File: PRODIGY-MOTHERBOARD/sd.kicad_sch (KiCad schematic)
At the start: 1 part, among them J13 Micro_SD_Card_Det2

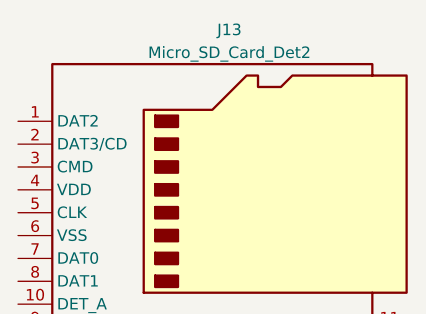
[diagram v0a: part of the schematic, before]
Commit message: project restructure done. Hierarchical sheet done. Outputs/breakouts sheet done
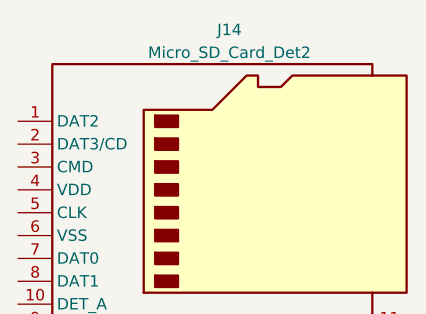
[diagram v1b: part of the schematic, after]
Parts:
- renumbered J13 to J14
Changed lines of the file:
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@@
-(kicad_sch (version 20230121) (generator eeschema)
-  (paper "A4")
-  (symbol (lib_id "Connector:Micro_SD_Card_Det2") (at 154.94 97.79 0) (unit 1)
-    (in_bom yes) (on_board yes) (dnp no) (fields_autoplaced)
-    (property "Reference" "J13" (at 155.575 77.47 0)
-      (effects (font (size 1.27 1.27)))
-    )
-    (property "Value" "Micro_SD_Card_Det2" (at 155.575 80.01 0)
-      (effects (font (size 1.27 1.27)))
-    )
-    (property "Footprint" "Connector_Card:microSD_HC_Hirose_DM3AT-SF-PEJM5" (at 207.01 80.01 0)
-      (effects (font (size 1.27 1.27)) hide)
-    )
-    (property "Datasheet" "https://www.hirose.com/en/product/document?clcode=&productname=&series=DM3&documenttype=Catalog&lang=en&documentid=D49662_en" (at 157.48 95.25 0)
-      (effects (font (size 1.27 1.27)) hide)
-    )
-    (property "JLCPCB" "" (at 154.94 97.79 0)
-      (effects (font (size 1.27 1.27)) hide)
-    )
-    (pin "1")
-    (pin "10")
-    (pin "11")
-    (pin "2")
-    (pin "3")
-    (pin "4")
-    (pin "5")
-    (pin "6")
-    (pin "7")
-    (pin "8")
-    (pin "9")
-    (instances
-      (project "PRODIGY-MOTHERBOARD"
-        (path "/f1c25860-8989-4190-bd24-2491d23ca7d9/33b59e3c-6456-4c33-9606-114445a2e2ee"
-          (reference "J13") (unit 1)
-        )
-      )
-    )
-  )
+(kicad_sch
+	(version 20231120)
+	(generator "eeschema")
+	(generator_version "8.0")
+	(paper "A4")
+	(symbol
+		(lib_id "Connector:Micro_SD_Card_Det2")
+		(at 154.94 97.79 0)
+		(unit 1)
+		(exclude_from_sim no)
+		(in_bom yes)
+		(on_board yes)
+		(dnp no)
+		(fields_autoplaced yes)
+		(property "Reference" "J14"
+			(at 155.575 77.47 0)
+			(effects
+				(font
+					(size 1.27 1.27)
+				)
+			)
+		)
+		(property "Value" "Micro_SD_Card_Det2"
+			(at 155.575 80.01 0)
+			(effects
+				(font
+					(size 1.27 1.27)
+				)
+			)
+		)
+		(property "Footprint" "Connector_Card:microSD_HC_Hirose_DM3AT-SF-PEJM5"
+			(at 207.01 80.01 0)
+			(effects
+				(font
+					(size 1.27 1.27)
+				)
+				(hide yes)
+			)
+		)
+		(property "Datasheet" "https://www.hirose.com/en/product/document?clcode=&productname=&series=DM3&documenttype=Catalog&lang=en&documentid=D49662_en"
+			(at 157.48 95.25 0)
+			(effects
+				(font
+					(size 1.27 1.27)
+				)
+				(hide yes)
+			)
+		)
+		(property "Description" ""
+			(at 154.94 97.79 0)
+			(effects
+				(font
+					(size 1.27 1.27)
+				)
+				(hide yes)
+			)
+		)
+		(property "JLCPCB" ""
+			(at 154.94 97.79 0)
+			(effects
+				(font
+					(size 1.27 1.27)
+				)
+				(hide yes)
+			)
+		)
+		(pin "1"
+		)
+		(pin "10"
+		)
+		(pin "11"
+		)
+		(pin "2"
+		)
+		(pin "3"
+		)
+		(pin "4"
+		)
+		(pin "5"
+		)
+		(pin "6"
+		)
+		(pin "7"
+		)
+		(pin "8"
+		)
+		(pin "9"
+		)
+		(instances
+			(project "PRODIGY-MOTHERBOARD"
+				(path "/f1c25860-8989-4190-bd24-2491d23ca7d9/e2913798-f444-47a6-8b64-53020d7d816b/c4f3c4b1-d676-4f7b-883c-6fdba835d106"
+					(reference "J14")
+					(unit 1)
+				)
+			)
+		)
+	)
 )

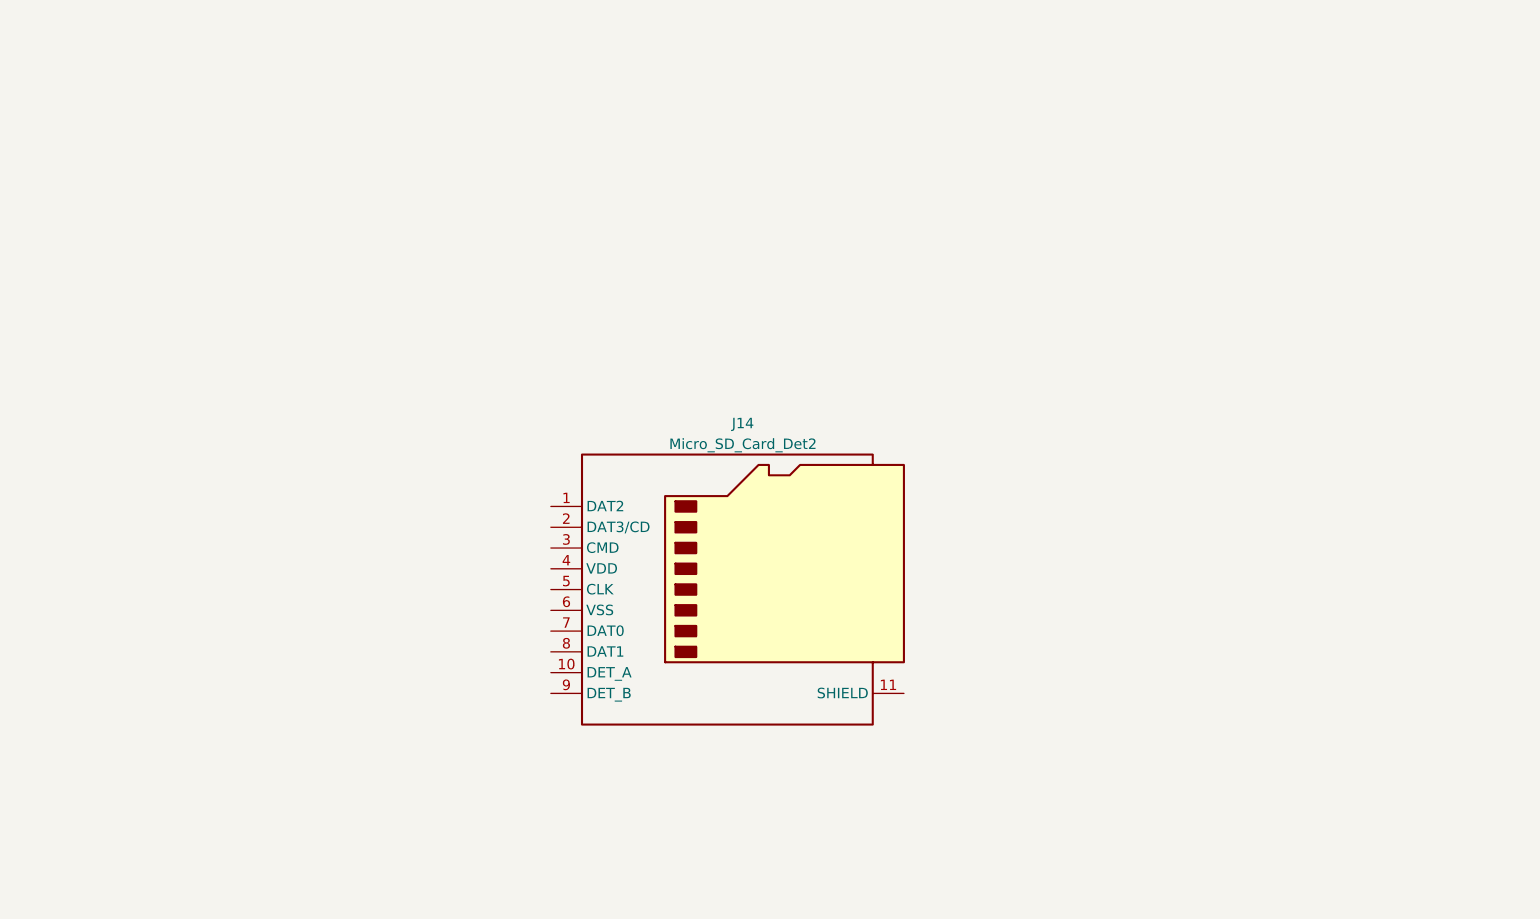
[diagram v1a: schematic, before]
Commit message: SPI SD CARD circuit added.
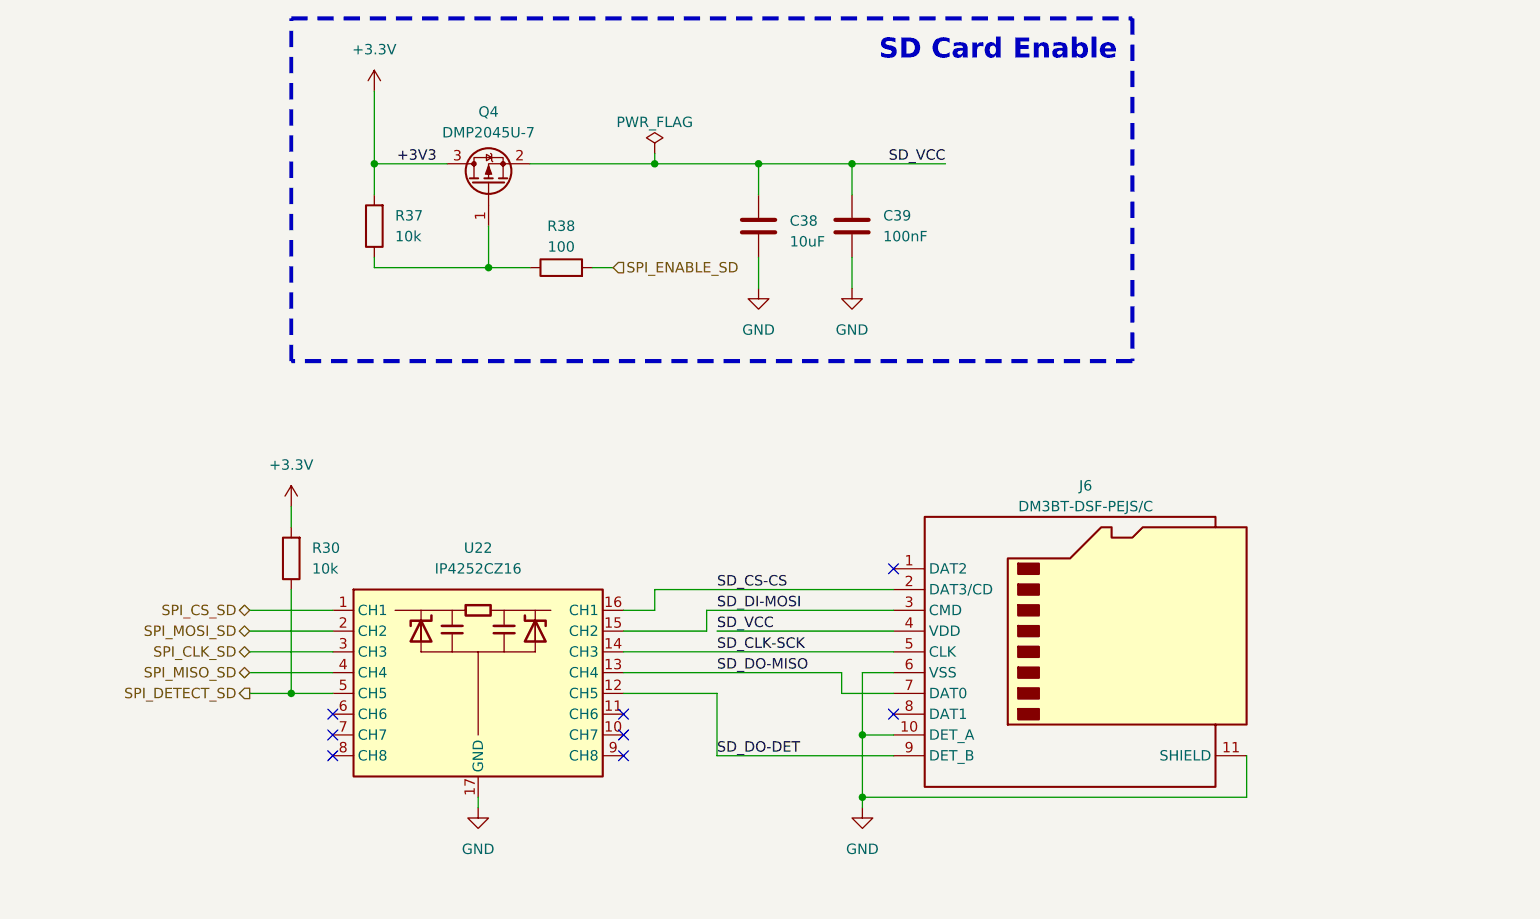
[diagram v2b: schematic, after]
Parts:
- removed J14: Micro_SD_Card_Det2, Connector_Card:microSD_HC_Hirose_DM3AT-SF-PEJM5, symbol Connector:Micro_SD_Card_Det2
- added C38: 10uF, Capacitor_SMD:C_1206_3216Metric, symbol Device:C
- added C39: 100nF, Capacitor_SMD:C_0805_2012Metric, symbol Device:C
- added J6: DM3BT-DSF-PEJS/C, Connector_Card:microSD_HC_Hirose_DM3BT-DSF-PEJS, symbol Connector:Micro_SD_Card_Det2
- added Q4: DMP2045U-7, Package_TO_SOT_SMD:SOT-23, symbol Transistor_FET:IRLML6402
- added R30, R37: 10k, Resistor_SMD:R_0603_1608Metric, symbol Device:R
- added R38: 100, Resistor_SMD:R_0603_1608Metric, symbol Device:R
- added U22: IP4252CZ16, Package_SON:Nexperia_HUSON-16_USON-16-1EP_1.35x3.3mm_P0.4mm_EP0.4x2.8mm, symbol Power_Protection:IP4252CZ16
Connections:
- new net: Q4.1 (G), R37.1, R38.1
- new net +3.3V: Q4.3 (D), R30.2, R37.2
- new net GND: C38.2, C39.2, J6.10 (DET_A), J6.11 (SHIELD), J6.6 (VSS), U22.17 (GND)
- new net SD_CLK-SCK: J6.5 (CLK), U22.14 (CH3)
- new net SD_CS-CS: J6.2 (DAT3/CD), U22.16 (CH1)
- new net SD_DI-MOSI: J6.3 (CMD), U22.15 (CH2)
- new net SD_DO-DET: J6.9 (DET_B), U22.12 (CH5)
- new net SD_DO-MISO: J6.7 (DAT0), U22.13 (CH4)
- new net SD_VCC: C38.1, C39.1, J6.4 (VDD), Q4.2 (S)
- new net SPI_CLK_SD: U22.3 (CH3)
- new net SPI_CS_SD: U22.1 (CH1)
- new net SPI_DETECT_SD: R30.1, U22.5 (CH5)
- new net SPI_ENABLE_SD: R38.2
- new net SPI_MISO_SD: U22.4 (CH4)
- new net SPI_MOSI_SD: U22.2 (CH2)
- no-connect marks 0 -> 8
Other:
- note added: "SD Card Enable"

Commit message: Finished neopixel and button's schematic.
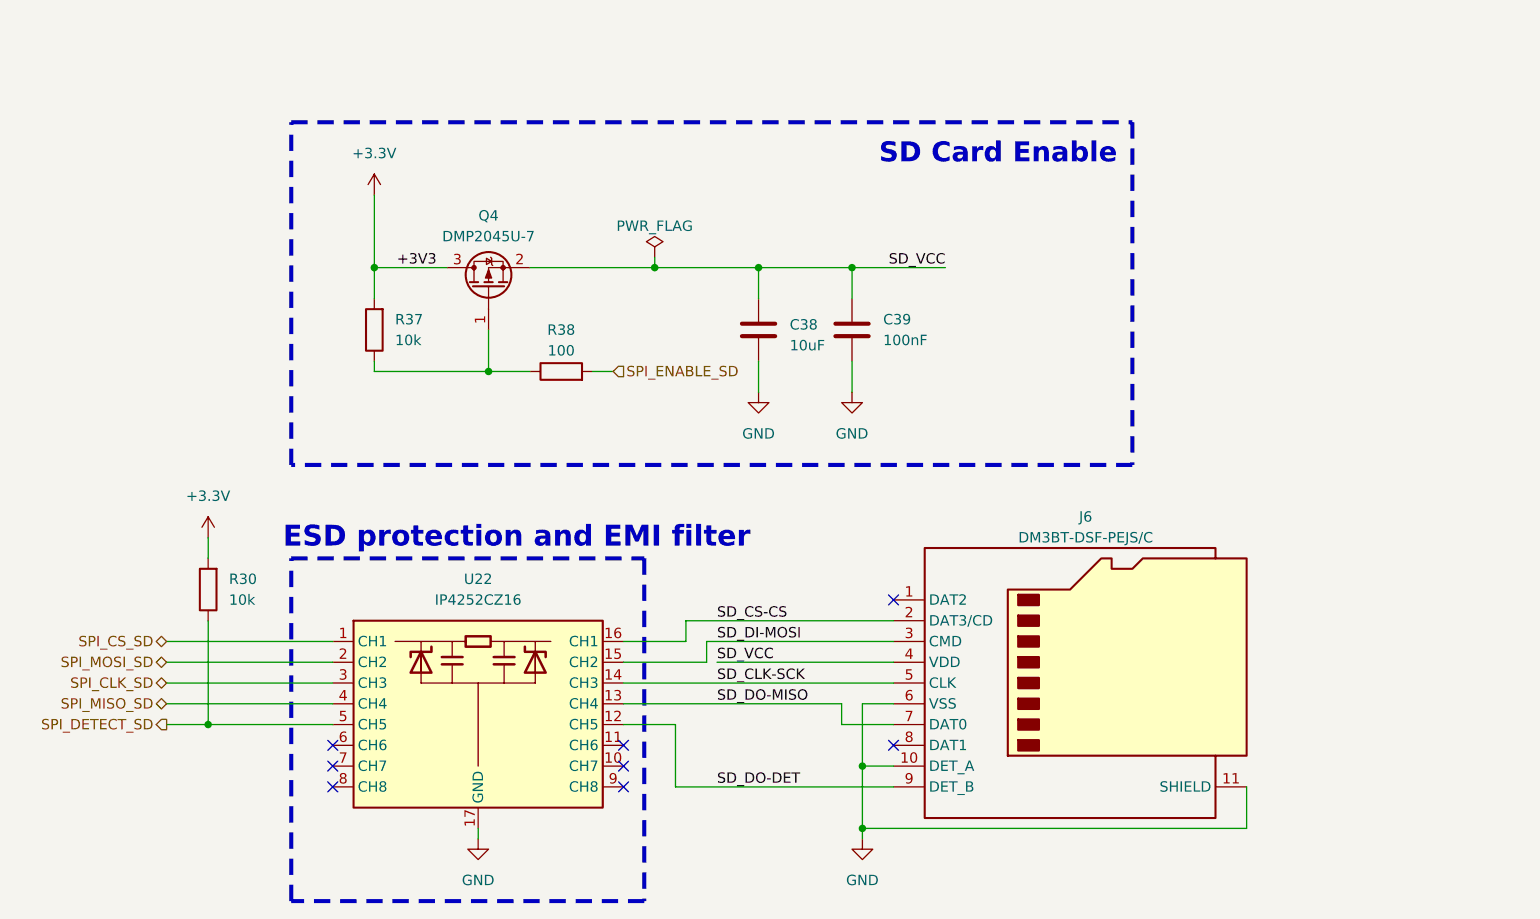
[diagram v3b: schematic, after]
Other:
- note added: "ESD protection and EMI filter"
- moved on the sheet: C38, C39, J6, Q4, R30, R37, R38, U22

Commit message: CAN schematic done
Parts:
- renumbered C38 to C4, C39 to C5, J6 to J22, Q4 to Q1, R30 to R6, R37 to R7, R38 to R8, U22 to U4
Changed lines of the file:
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@@
 		(dnp no)
 		(fields_autoplaced yes)
-		(property "Reference" "#PWR079"
+		(property "Reference" "#PWR021"
 			(at 123.19 134.62 0)
 			(effects
@@
 			(project "PRODIGY-MOTHERBOARD"
 				(path "/f1c25860-8989-4190-bd24-2491d23ca7d9/e2913798-f444-47a6-8b64-53020d7d816b/c4f3c4b1-d676-4f7b-883c-6fdba835d106"
-					(reference "#PWR079")
+					(reference "#PWR021")
 					(unit 1)
 				)
@@
 		(dnp no)
 		(fields_autoplaced yes)
-		(property "Reference" "R38"
+		(property "Reference" "R8"
 			(at 133.35 66.04 90)
 			(effects
@@
 			(project "PRODIGY-MOTHERBOARD"
 				(path "/f1c25860-8989-4190-bd24-2491d23ca7d9/e2913798-f444-47a6-8b64-53020d7d816b/c4f3c4b1-d676-4f7b-883c-6fdba835d106"
-					(reference "R38")
+					(reference "R8")
 					(unit 1)
 				)
@@
 		(dnp no)
 		(fields_autoplaced yes)
-		(property "Reference" "R37"
+		(property "Reference" "R7"
 			(at 113.03 64.7699 0)
 			(effects
@@
 			(project "PRODIGY-MOTHERBOARD"
 				(path "/f1c25860-8989-4190-bd24-2491d23ca7d9/e2913798-f444-47a6-8b64-53020d7d816b/c4f3c4b1-d676-4f7b-883c-6fdba835d106"
-					(reference "R37")
+					(reference "R7")
 					(unit 1)
 				)
@@
 		(dnp no)
 		(fields_autoplaced yes)
-		(property "Reference" "#PWR084"
+		(property "Reference" "#PWR020"
 			(at 110.49 53.34 0)
 			(effects
@@
 			(project "PRODIGY-MOTHERBOARD"
 				(path "/f1c25860-8989-4190-bd24-2491d23ca7d9/e2913798-f444-47a6-8b64-53020d7d816b/c4f3c4b1-d676-4f7b-883c-6fdba835d106"
-					(reference "#PWR084")
+					(reference "#PWR020")
 					(unit 1)
 				)
@@
 		(dnp no)
 		(fields_autoplaced yes)
-		(property "Reference" "#PWR081"
+		(property "Reference" "#PWR019"
 			(at 90.17 95.25 0)
 			(effects
@@
 			(project "PRODIGY-MOTHERBOARD"
 				(path "/f1c25860-8989-4190-bd24-2491d23ca7d9/e2913798-f444-47a6-8b64-53020d7d816b/c4f3c4b1-d676-4f7b-883c-6fdba835d106"
-					(reference "#PWR081")
+					(reference "#PWR019")
 					(unit 1)
 				)
@@
 		(dnp no)
 		(fields_autoplaced yes)
-		(property "Reference" "Q4"
+		(property "Reference" "Q1"
 			(at 124.46 52.07 90)
 			(effects
@@
 			(project "PRODIGY-MOTHERBOARD"
 				(path "/f1c25860-8989-4190-bd24-2491d23ca7d9/e2913798-f444-47a6-8b64-53020d7d816b/c4f3c4b1-d676-4f7b-883c-6fdba835d106"
-					(reference "Q4")
+					(reference "Q1")
 					(unit 1)
 				)
@@
 		(dnp no)
 		(fields_autoplaced yes)
-		(property "Reference" "#FLG03"
+		(property "Reference" "#FLG01"
 			(at 144.78 55.245 0)
 			(effects
@@
 			(project "PRODIGY-MOTHERBOARD"
 				(path "/f1c25860-8989-4190-bd24-2491d23ca7d9/e2913798-f444-47a6-8b64-53020d7d816b/c4f3c4b1-d676-4f7b-883c-6fdba835d106"
-					(reference "#FLG03")
+					(reference "#FLG01")
 					(unit 1)
 				)
@@
 		(dnp no)
 		(fields_autoplaced yes)
-		(property "Reference" "#PWR083"
+		(property "Reference" "#PWR023"
 			(at 168.91 80.01 0)
 			(effects
@@
 			(project "PRODIGY-MOTHERBOARD"
 				(path "/f1c25860-8989-4190-bd24-2491d23ca7d9/e2913798-f444-47a6-8b64-53020d7d816b/c4f3c4b1-d676-4f7b-883c-6fdba835d106"
-					(reference "#PWR083")
+					(reference "#PWR023")
 					(unit 1)
 				)
@@
 		(dnp no)
 		(fields_autoplaced yes)
-		(property "Reference" "#PWR080"
+		(property "Reference" "#PWR024"
 			(at 170.18 134.62 0)
 			(effects
@@
 			(project "PRODIGY-MOTHERBOARD"
 				(path "/f1c25860-8989-4190-bd24-2491d23ca7d9/e2913798-f444-47a6-8b64-53020d7d816b/c4f3c4b1-d676-4f7b-883c-6fdba835d106"
-					(reference "#PWR080")
+					(reference "#PWR024")
 					(unit 1)
 				)
@@
 		(dnp no)
 		(fields_autoplaced yes)
-		(property "Reference" "C38"
+		(property "Reference" "C4"
 			(at 161.29 65.405 0)
 			(effects
@@
 			(project "PRODIGY-MOTHERBOARD"
 				(path "/f1c25860-8989-4190-bd24-2491d23ca7d9/e2913798-f444-47a6-8b64-53020d7d816b/c4f3c4b1-d676-4f7b-883c-6fdba835d106"
-					(reference "C38")
+					(reference "C4")
 					(unit 1)
 				)
@@
 		(dnp no)
 		(fields_autoplaced yes)
-		(property "Reference" "#PWR082"
+		(property "Reference" "#PWR022"
 			(at 157.48 80.01 0)
 			(effects
@@
 			(project "PRODIGY-MOTHERBOARD"
 				(path "/f1c25860-8989-4190-bd24-2491d23ca7d9/e2913798-f444-47a6-8b64-53020d7d816b/c4f3c4b1-d676-4f7b-883c-6fdba835d106"
-					(reference "#PWR082")
+					(reference "#PWR022")
 					(unit 1)
 				)
@@
 		(dnp no)
 		(fields_autoplaced yes)
-		(property "Reference" "R30"
+		(property "Reference" "R6"
 			(at 92.71 96.5199 0)
 			(effects
@@
 			(project "PRODIGY-MOTHERBOARD"
 				(path "/f1c25860-8989-4190-bd24-2491d23ca7d9/e2913798-f444-47a6-8b64-53020d7d816b/c4f3c4b1-d676-4f7b-883c-6fdba835d106"
-					(reference "R30")
+					(reference "R6")
 					(unit 1)
 				)
@@
 		(dnp no)
 		(fields_autoplaced yes)
-		(property "Reference" "C39"
+		(property "Reference" "C5"
 			(at 172.72 64.7699 0)
 			(effects
@@
 			(project "PRODIGY-MOTHERBOARD"
 				(path "/f1c25860-8989-4190-bd24-2491d23ca7d9/e2913798-f444-47a6-8b64-53020d7d816b/c4f3c4b1-d676-4f7b-883c-6fdba835d106"
-					(reference "C39")
+					(reference "C5")
 					(unit 1)
 				)
@@
 		(on_board yes)
 		(dnp no)
-		(property "Reference" "J6"
+		(property "Reference" "J22"
 			(at 197.485 88.9 0)
 			(effects
@@
 			(project "PRODIGY-MOTHERBOARD"
 				(path "/f1c25860-8989-4190-bd24-2491d23ca7d9/e2913798-f444-47a6-8b64-53020d7d816b/c4f3c4b1-d676-4f7b-883c-6fdba835d106"
-					(reference "J6")
+					(reference "J22")
 					(unit 1)
 				)
@@
 		(dnp no)
 		(fields_autoplaced yes)
-		(property "Reference" "U22"
+		(property "Reference" "U4"
 			(at 123.19 96.52 0)
 			(effects
@@
 			(project "PRODIGY-MOTHERBOARD"
 				(path "/f1c25860-8989-4190-bd24-2491d23ca7d9/e2913798-f444-47a6-8b64-53020d7d816b/c4f3c4b1-d676-4f7b-883c-6fdba835d106"
-					(reference "U22")
-					(unit 1)
-				)
+					(reference "U4")
+					(unit 1)
+				)
